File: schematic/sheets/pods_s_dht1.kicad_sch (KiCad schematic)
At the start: 4 parts, among them J3 LIGHT-SENS-1x03

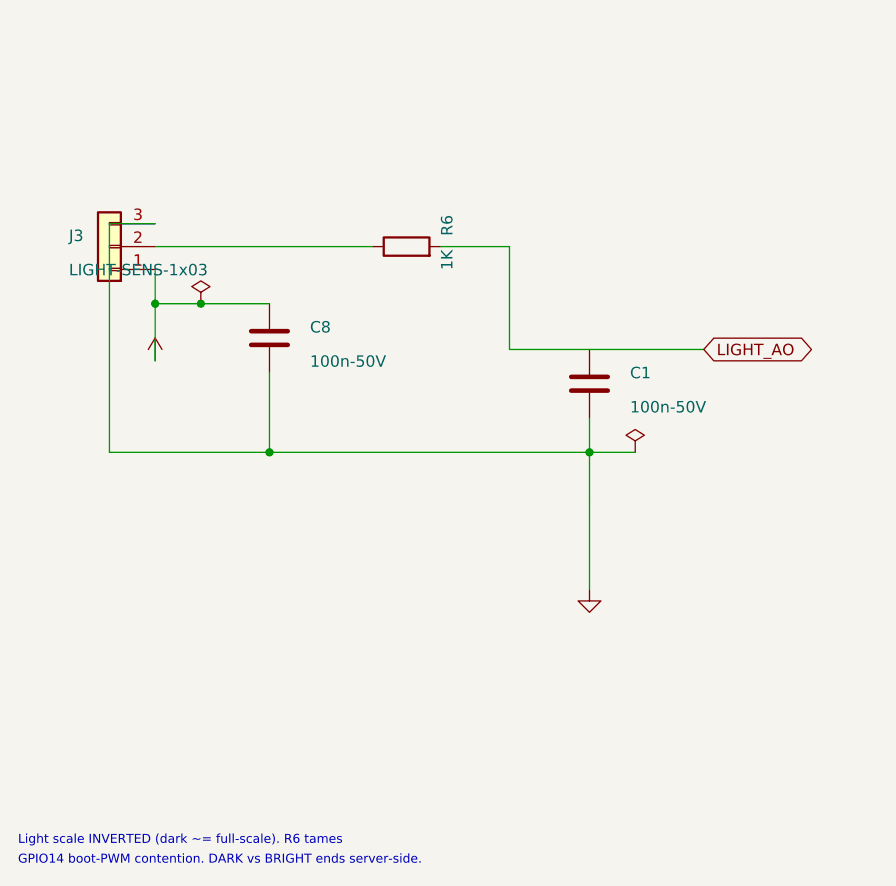
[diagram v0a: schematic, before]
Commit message: Organize schematic/: sheets/ mfg/ final/, drop sklib
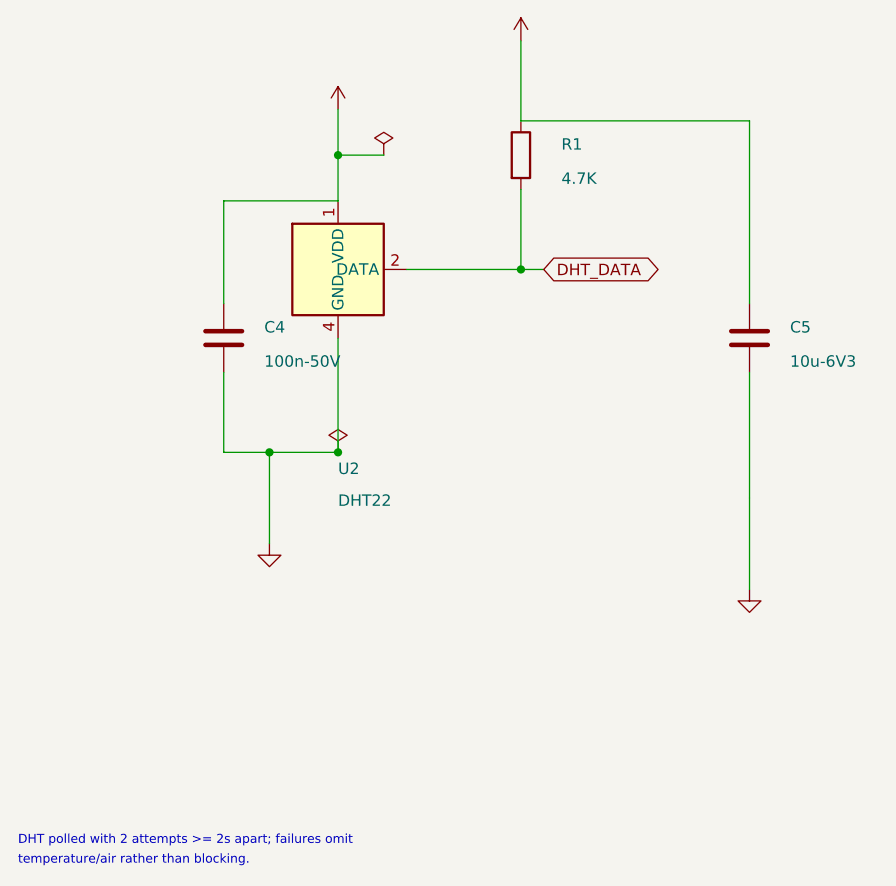
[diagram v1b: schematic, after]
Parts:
- removed C1, C8: 100n-50V, Capacitor_SMD:C_0603_1608Metric, symbol Device:C
- removed J3: LIGHT-SENS-1x03, Connector_PinHeader_2.54mm:PinHeader_1x03_P2.54mm_Vertical, symbol Connector_Generic:Conn_01x03
- removed R6: 1K, Resistor_SMD:R_0603_1608Metric, symbol Device:R
- added C4: 100n-50V, Capacitor_SMD:C_0603_1608Metric, symbol Device:C
- added C5: 10u-6V3, Capacitor_SMD:C_0603_1608Metric, symbol Device:C
- added R1: 4.7K, Resistor_SMD:R_0603_1608Metric, symbol Device:R
- added U2: DHT22, Connector_PinHeader_2.54mm:PinHeader_1x04_P2.54mm_Vertical, symbol Sensor:DHT11
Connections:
- net +3V3: now also C4.1, C5.1, R1.1, U2.1 (VDD)
- net GND: now also C4.2, C5.2, U2.4 (GND)
- new net DHT_DATA: R1.2, U2.2 (DATA)
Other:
- note added: "DHT polled with 2 attempts >= 2s apart; failures omit"
- note added: "temperature/air rather than blocking."
- note removed: "GPIO14 boot-PWM contention. DARK vs BRIGHT ends server-side."
- note removed: "Light scale INVERTED (dark ~= full-scale). R6 tames"
